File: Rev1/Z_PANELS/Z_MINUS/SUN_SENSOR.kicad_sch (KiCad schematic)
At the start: 25 parts, among them Q10 BSS138, Q11 BSS138, Q13 BSS138, Q14 BSS138, U2 OPT4001DTST

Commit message: changed resistor sizes;
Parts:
- added IC1: LTC4316IDD#PBF, SON50P300X300X85-11N-D, symbol AA_AUTO_LOADER:LTC4316IDD#PBF
- added R? (x4): 10K, Resistor_SMD:R_0805_2012Metric, symbol Device:R_US
- added R?: 280k, Resistor_SMD:R_0805_2012Metric, symbol Device:R_US
- added R?: 1000k, Resistor_SMD:R_0805_2012Metric, symbol Device:R_US
- R? (x8): footprint Resistor_SMD:R_0603_1608Metric -> Resistor_SMD:R_0805_2012Metric
- R? (x2): footprint Resistor_SMD:R_0402_1005Metric -> Resistor_SMD:R_0805_2012Metric
- renumbered Q10 to Q1, Q11 to Q2, Q13 to Q4, Q14 to Q5, U2 to U1
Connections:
- net +3.3V: now also IC1.4 (VCC), IC1.5 (ENABLE), R?.1, R?.2, R?.2, R?.2, R?.2
- net GND: now also IC1.1 (GND_1), IC1.11 (GND_2), IC1.2 (XORH), R?.2
- net SCL_SUN: now also IC1.10 (SCLIN), R?.1; no longer JP1.3 (B), U1.5 (SCL)
- net SDA_SUN: now also IC1.9 (SCLOUT), R?.1; no longer JP1.1 (A), U1.8 (SDA)
- new net: IC1.3 (XORL), R?.1, R?.2
- new net SCL_4001: IC1.7 (SDAIN), JP1.3 (B), R?.1, U1.5 (SCL)
- new net SDA_4001: IC1.8 (SDAOUT), JP1.1 (A), R?.1, U1.8 (SDA)
- no-connect marks 0 -> 4
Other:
- note added: "i2c address 0x42"

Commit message: made changes to Z minus and Z plus cutouts
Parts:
- R? (x2): now not fitted; now left out of the parts list
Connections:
- net GND: now also Q1.2 (S), Q2.2 (S), Q4.2 (S), Q5.2 (S); no longer Q1.3 (D), Q2.3 (D), Q4.3 (D), Q5.3 (D)
- net at Q4.1 (G), R?.1: now also Q5.3 (D); no longer Q5.2 (S)
- net at Q?.5 (B2), R?.2, R?.2: now also Q4.3 (D); no longer Q4.2 (S)
- net at Q1.1 (G), R?.1: now also Q2.3 (D); no longer Q2.2 (S)
- net at Q?.5 (B2), R?.1, R?.2: now also Q1.3 (D); no longer Q1.2 (S)
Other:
- moved on the sheet: Q1, Q2, Q4, Q5

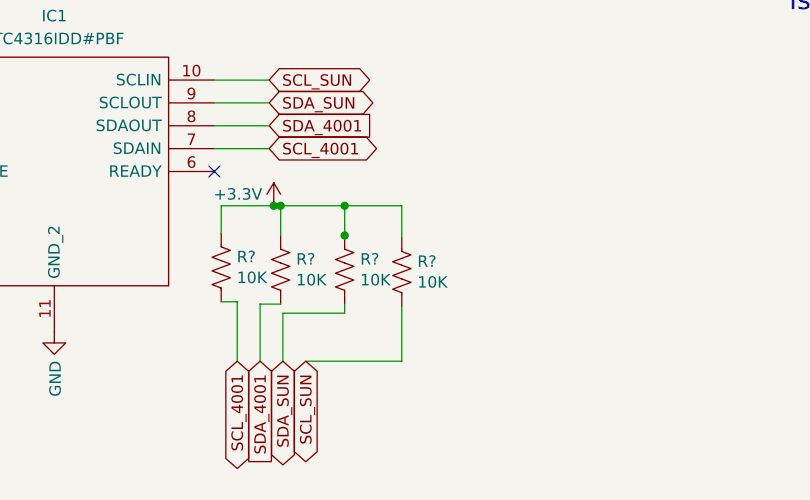
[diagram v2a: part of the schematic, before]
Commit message: finished Z minus board design
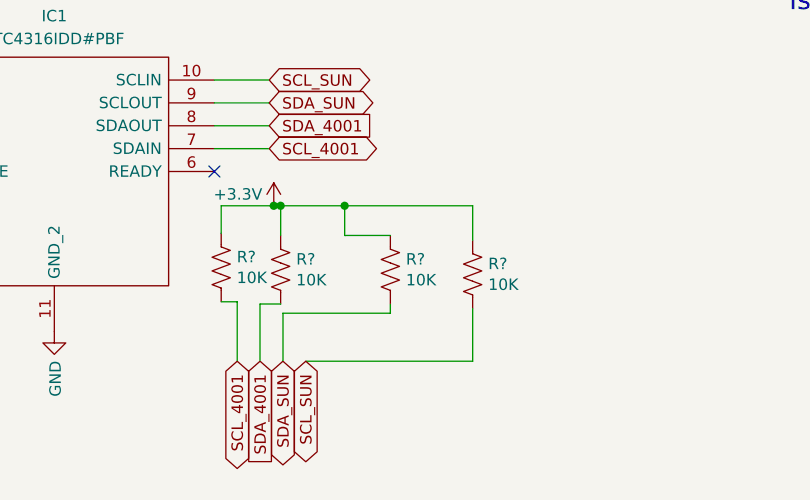
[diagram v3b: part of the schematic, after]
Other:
- moved on the sheet: R?
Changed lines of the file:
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@@
   (junction (at 195.834 96.266) (diameter 0) (color 0 0 0 0)
-  )
-  (junction (at 123.19 134.874) (diameter 0) (color 0 0 0 0)
   )
   (junction (at 216.154 91.186) (diameter 0) (color 0 0 0 0)
@@
     (stroke (width 0) (type default))
   )
-  (wire (pts (xy 123.444 134.874) (xy 123.19 134.874))
+  (wire (pts (xy 123.19 134.874) (xy 128.27 134.874))
     (stroke (width 0) (type default))
   )
@@
     (stroke (width 0) (type default))
   )
-  (wire (pts (xy 118.872 148.844) (xy 129.54 148.844))
+  (wire (pts (xy 118.872 148.844) (xy 137.414 148.844))
     (stroke (width 0) (type default))
   )
@@
     (stroke (width 0) (type default))
   )
-  (wire (pts (xy 129.54 131.572) (xy 129.54 135.128))
+  (wire (pts (xy 137.414 131.572) (xy 137.414 135.382))
     (stroke (width 0) (type default))
   )
@@
     (stroke (width 0) (type default))
   )
-  (wire (pts (xy 123.19 142.494) (xy 123.19 143.51))
-    (stroke (width 0) (type default))
-  )
-  (wire (pts (xy 123.19 131.572) (xy 129.54 131.572))
+  (wire (pts (xy 128.27 142.494) (xy 128.27 143.51))
+    (stroke (width 0) (type default))
+  )
+  (wire (pts (xy 123.19 131.572) (xy 137.414 131.572))
     (stroke (width 0) (type default))
   )
@@
     (stroke (width 0) (type default))
   )
-  (wire (pts (xy 123.19 143.51) (xy 116.332 143.51))
+  (wire (pts (xy 128.27 143.51) (xy 116.332 143.51))
     (stroke (width 0) (type default))
   )
@@
     (stroke (width 0) (type default))
   )
-  (wire (pts (xy 129.54 148.844) (xy 129.54 142.748))
+  (wire (pts (xy 137.414 148.844) (xy 137.414 143.002))
     (stroke (width 0) (type default))
   )
@@
     )
   )
-  (symbol (lib_id "Device:R_US") (at 129.54 138.938 180) (unit 1)
-    (in_bom yes) (on_board yes) (dnp no)
-    (property "Reference" "R?" (at 131.2672 137.7696 0)
-      (effects (font (size 1.27 1.27)) (justify right))
-    )
-    (property "Value" "10K" (at 131.2672 140.081 0)
-      (effects (font (size 1.27 1.27)) (justify right))
-    )
-    (property "Footprint" "Resistor_SMD:R_0805_2012Metric" (at 128.524 138.684 90)
-      (effects (font (size 1.27 1.27)) hide)
-    )
-    (property "Datasheet" "~" (at 129.54 138.938 0)
-      (effects (font (size 1.27 1.27)) hide)
-    )
-    (property "Field4" "" (at 129.54 138.938 0)
+  (symbol (lib_id "Device:R_US") (at 137.414 139.192 180) (unit 1)
+    (in_bom yes) (on_board yes) (dnp no)
+    (property "Reference" "R?" (at 139.1412 138.0236 0)
+      (effects (font (size 1.27 1.27)) (justify right))
+    )
+    (property "Value" "10K" (at 139.1412 140.335 0)
+      (effects (font (size 1.27 1.27)) (justify right))
+    )
+    (property "Footprint" "Resistor_SMD:R_0805_2012Metric" (at 136.398 138.938 90)
+      (effects (font (size 1.27 1.27)) hide)
+    )
+    (property "Datasheet" "~" (at 137.414 139.192 0)
+      (effects (font (size 1.27 1.27)) hide)
+    )
+    (property "Field4" "" (at 137.414 139.192 0)
       (effects (font (size 1.27 1.27)) hide)
     )
@@
     )
   )
-  (symbol (lib_id "Device:R_US") (at 123.19 138.684 180) (unit 1)
-    (in_bom yes) (on_board yes) (dnp no)
-    (property "Reference" "R?" (at 124.9172 137.5156 0)
-      (effects (font (size 1.27 1.27)) (justify right))
-    )
-    (property "Value" "10K" (at 124.9172 139.827 0)
-      (effects (font (size 1.27 1.27)) (justify right))
-    )
-    (property "Footprint" "Resistor_SMD:R_0805_2012Metric" (at 122.174 138.43 90)
-      (effects (font (size 1.27 1.27)) hide)
-    )
-    (property "Datasheet" "~" (at 123.19 138.684 0)
-      (effects (font (size 1.27 1.27)) hide)
-    )
-    (property "Field4" "" (at 123.19 138.684 0)
-      (effects (font (size 1.27 1.27)) hide)
-    )
+  (symbol (lib_id "Device:R_US") (at 128.27 138.684 180) (unit 1)
+    (in_bom yes) (on_board yes) (dnp no)
+    (property "Reference" "R?" (at 129.9972 137.5156 0)
+      (effects (font (size 1.27 1.27)) (justify right))
+    )
+    (property "Value" "10K" (at 129.9972 139.827 0)
+      (effects (font (size 1.27 1.27)) (justify right))
+    )
+    (property "Footprint" "Resistor_SMD:R_0805_2012Metric" (at 127.254 138.43 90)
+      (effects (font (size 1.27 1.27)) hide)
+    )
+    (property "Datasheet" "~" (at 128.27 138.684 0)
+      (effects (font (size 1.27 1.27)) hide)
+    )
+    (property "Field4" "" (at 128.27 138.684 0)
+      (effects (font (size 1.27 1.27)) hide)
+    )

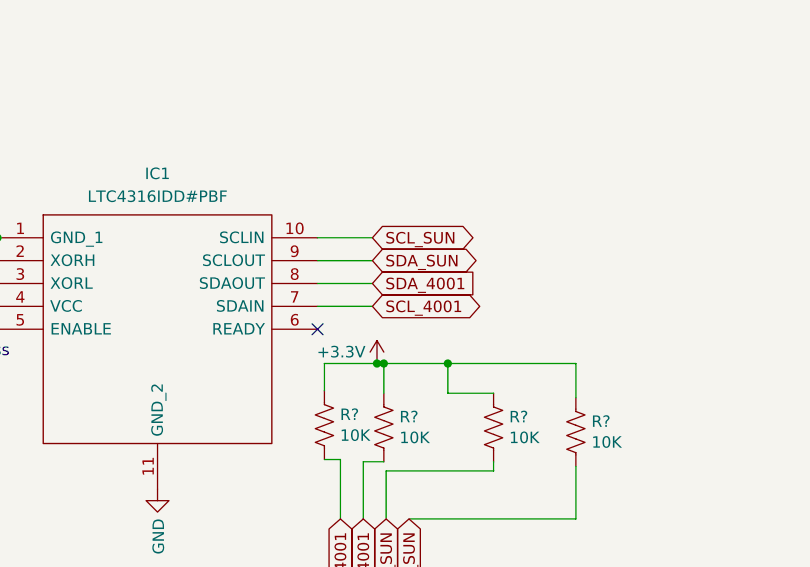
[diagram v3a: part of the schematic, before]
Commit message: fixed bug in Z minus
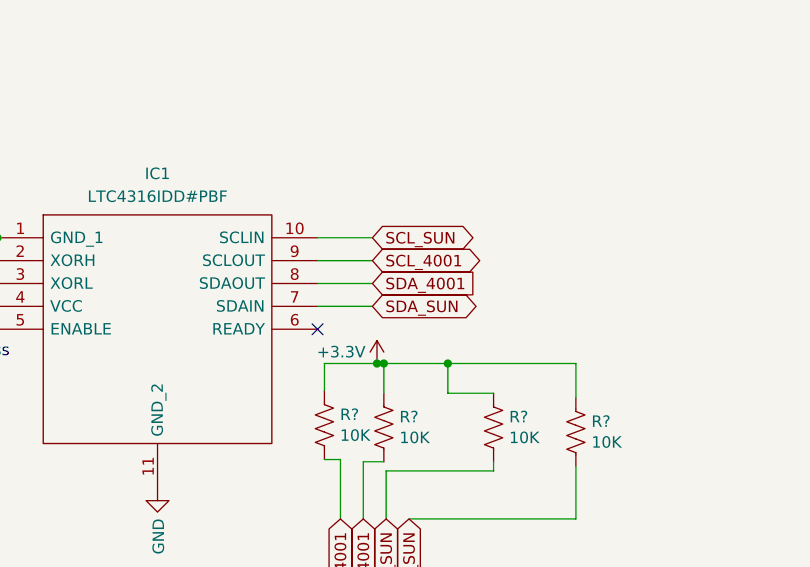
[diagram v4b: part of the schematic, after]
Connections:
- net SCL_4001: now also IC1.9 (SCLOUT); no longer IC1.7 (SDAIN)
- net SDA_SUN: now also IC1.7 (SDAIN); no longer IC1.9 (SCLOUT)
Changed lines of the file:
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@@
-    (stroke (width 0) (type default))
-  )
-  (wire (pts (xy 114.808 120.142) (xy 108.712 120.142))
     (stroke (width 0) (type default))
   )
@@
     (stroke (width 0) (type default))
   )
+  (wire (pts (xy 108.712 125.222) (xy 114.808 125.222))
+    (stroke (width 0) (type default))
+  )
   (wire (pts (xy 70.104 125.222) (xy 73.152 125.222))
     (stroke (width 0) (type default))
@@
     (stroke (width 0) (type default))
   )
-  (wire (pts (xy 114.808 125.222) (xy 108.712 125.222))
-    (stroke (width 0) (type default))
-  )
   (wire (pts (xy 45.974 69.342) (xy 48.006 69.342))
     (stroke (width 0) (type default))
@@
   )
   (wire (pts (xy 225.298 96.52) (xy 225.298 96.266))
+    (stroke (width 0) (type default))
+  )
+  (wire (pts (xy 108.712 120.142) (xy 114.808 120.142))
     (stroke (width 0) (type default))
   )
@@
     )
   )
-  (global_label "SDA_SUN" (shape bidirectional) (at 114.808 120.142 0)
+  (global_label "SDA_SUN" (shape bidirectional) (at 114.808 125.222 0)
     (effects (font (size 1.27 1.27)) (justify left))
-    (property "Intersheetrefs" "${INTERSHEET_REFS}" (at 114.808 120.142 0)
+    (property "Intersheetrefs" "${INTERSHEET_REFS}" (at 114.808 125.222 0)
       (effects (font (size 1.27 1.27)) hide)
     )
@@
     )
   )
-  (global_label "SCL_4001" (shape bidirectional) (at 114.808 125.222 0)
+  (global_label "SCL_4001" (shape bidirectional) (at 114.808 120.142 0)
     (effects (font (size 1.27 1.27)) (justify left))
-    (property "Intersheetrefs" "${INTERSHEET_REFS}" (at 114.808 125.222 0)
-      (effects (font (size 1.27 1.27)) hide)
-    )
+    (property "Intersheetrefs" "${INTERSHEET_REFS}" (at 114.808 120.142 0)
+      (effects (font (size 1.27 1.27)) hide)
+    )

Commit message: fixed bugs and finished Z plus
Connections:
- net +3.3v is gone; now on net +3.3V: JP2.3 (B), U1.1 (VDD)
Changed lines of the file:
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@@
+    )
+  )
+  (symbol (lib_id "power:+3.3V") (at 52.578 81.534 0) (mirror y) (unit 1)
+    (in_bom yes) (on_board yes) (dnp no)
+    (property "Reference" "#PWR?" (at 52.578 85.344 0)
+      (effects (font (size 1.27 1.27)) hide)
+    )
+    (property "Value" "+3.3V" (at 51.308 80.264 0)
+      (effects (font (size 1.27 1.27)) (justify left))
+    )
+    (property "Footprint" "" (at 52.578 81.534 0)
+      (effects (font (size 1.27 1.27)) hide)
+    )
+    (property "Datasheet" "" (at 52.578 81.534 0)
+      (effects (font (size 1.27 1.27)) hide)
+    )
+    (pin "1")
+    (instances
+      (project "xpanel"
+        (path "/30bf83b4-3f3b-46f2-ac0f-8077e2dc1b24"
+          (reference "#PWR?") (unit 1)
+        )
+      )
+      (project "Z_MINUS_REV1"
+        (path "/39cf28b0-d395-4333-bc0e-a98538893595/02f51ab8-9bf5-460b-98ef-c53969a9f1c8"
+          (reference "#PWR031") (unit 1)
+        )
+      )
+      (project "Xpanel_V1_final"
+        (path "/97119169-578f-44be-8822-faf8f0e4fcd6"
+          (reference "#PWR011") (unit 1)
+        )
+        (path "/97119169-578f-44be-8822-faf8f0e4fcd6/db306d3f-1ab7-4e38-afab-c78bdb56c587"
+          (reference "#PWR031") (unit 1)
+        )
+        (path "/97119169-578f-44be-8822-faf8f0e4fcd6/06756695-4e8e-4b7d-905d-85546769f1f1"
+          (reference "#PWR031") (unit 1)
+        )
+      )
+    )
+  )
+  (symbol (lib_id "power:+3.3V") (at 54.61 64.008 0) (mirror y) (unit 1)
+    (in_bom yes) (on_board yes) (dnp no)
+    (property "Reference" "#PWR?" (at 54.61 67.818 0)
+      (effects (font (size 1.27 1.27)) hide)
+    )
+    (property "Value" "+3.3V" (at 53.34 62.738 0)
+      (effects (font (size 1.27 1.27)) (justify left))
+    )
+    (property "Footprint" "" (at 54.61 64.008 0)
+      (effects (font (size 1.27 1.27)) hide)
+    )
+    (property "Datasheet" "" (at 54.61 64.008 0)
+      (effects (font (size 1.27 1.27)) hide)
+    )
+    (pin "1")
+    (instances
+      (project "xpanel"
+        (path "/30bf83b4-3f3b-46f2-ac0f-8077e2dc1b24"
+          (reference "#PWR?") (unit 1)
+        )
+      )
+      (project "Z_MINUS_REV1"
+        (path "/39cf28b0-d395-4333-bc0e-a98538893595/02f51ab8-9bf5-460b-98ef-c53969a9f1c8"
+          (reference "#PWR030") (unit 1)
+        )
+      )
+      (project "Xpanel_V1_final"
+        (path "/97119169-578f-44be-8822-faf8f0e4fcd6"
+          (reference "#PWR011") (unit 1)
+        )
+        (path "/97119169-578f-44be-8822-faf8f0e4fcd6/db306d3f-1ab7-4e38-afab-c78bdb56c587"
+          (reference "#PWR031") (unit 1)
+        )
+        (path "/97119169-578f-44be-8822-faf8f0e4fcd6/06756695-4e8e-4b7d-905d-85546769f1f1"
+          (reference "#PWR031") (unit 1)
+        )
+      )
     )
   )

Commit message: updated boards
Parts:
- added C4 (x2): 0.1uF, Capacitor_SMD:C_0805_2012Metric, symbol PCM_Capacitor_AKL:C_0805
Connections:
- net +3.3V: now also C4.1, C4.1
- net GND: now also C4.2, C4.2
